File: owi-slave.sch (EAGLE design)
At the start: 6 parts, among them IC1 AT90S2313P

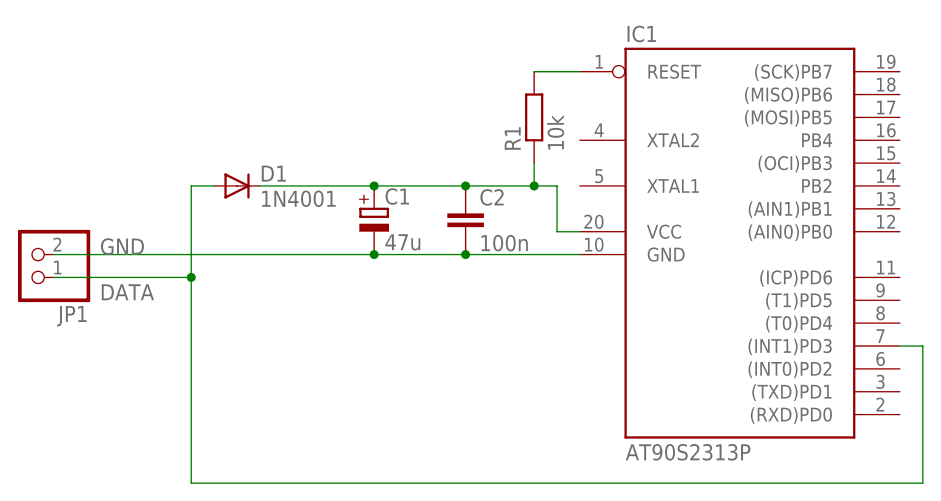
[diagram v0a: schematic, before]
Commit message: update readme and schematic (no bus-powered application at the moment)
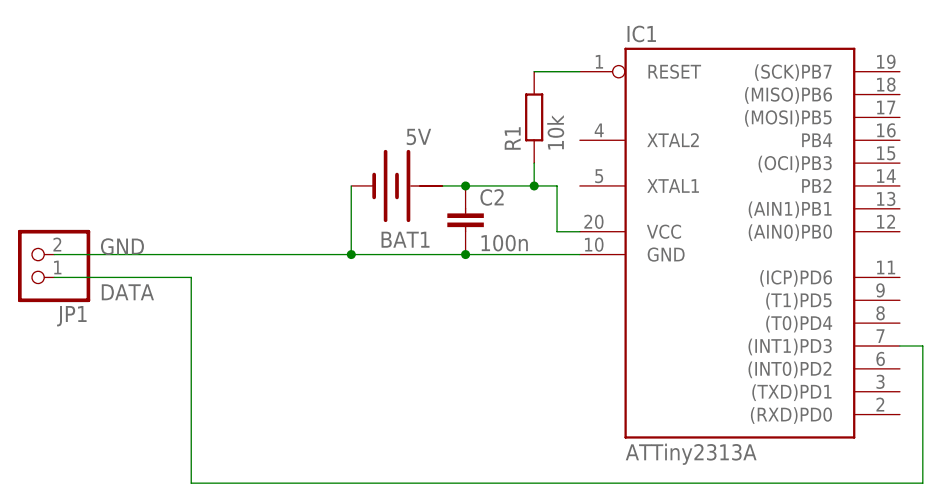
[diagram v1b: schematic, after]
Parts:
- removed C1: 47u, rcl:CPOL-EUE2,5-6E
- removed D1: 1N4001, diode:1N4004
- added BAT1: 5V, special:BATTERY
- IC1: value AT90S2313P -> ATTiny2313A
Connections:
- net DATA: no longer D1.A
- net GND: now also BAT1.-; no longer C1.-
- net N$1: now also BAT1.+; no longer C1.+, D1.C
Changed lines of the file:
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@@
 <?xml version="1.0" encoding="utf-8"?>
 <!DOCTYPE eagle SYSTEM "eagle.dtd">
-<eagle version="6.5.0">
+<eagle version="6.6.0">
 <drawing>
 <settings>
@@
 </classes>
 <parts>
-<part name="IC1" library="atmel" deviceset="AT90S2313" device="P"/>
-<part name="C1" library="rcl" deviceset="CPOL-EU" device="E2,5-6E" value="47u"/>
+<part name="IC1" library="atmel" deviceset="AT90S2313" device="P" value="ATTiny2313A"/>
 <part name="C2" library="resistor" deviceset="C-EU" device="025-024X044" value="100n"/>
-<part name="D1" library="diode" deviceset="1N4004" device="" value="1N4001"/>
 <part name="JP1" library="pinhead" deviceset="PINHD-1X2" device=""/>
 <part name="R1" library="resistor" deviceset="R-EU_" device="0207/10" value="10k"/>
+<part name="BAT1" library="special" deviceset="BATTERY" device="" value="5V"/>
 </parts>
 <sheets>
@@
 <instances>
 <instance part="IC1" gate="G$1" x="66.04" y="60.96"/>
-<instance part="C1" gate="G$1" x="25.4" y="66.04"/>
 <instance part="C2" gate="G$1" x="35.56" y="66.04"/>
-<instance part="D1" gate="1" x="10.16" y="68.58"/>
 <instance part="JP1" gate="G$1" x="-12.7" y="60.96" rot="R180"/>
 <instance part="R1" gate="G$1" x="43.18" y="76.2" rot="R90"/>
+<instance part="BAT1" gate="G$1" x="27.94" y="68.58" rot="R180"/>
 </instances>
 <busses>
@@
 <net name="N$1" class="0">
 <segment>
-<pinref part="D1" gate="1" pin="C"/>
-<pinref part="C1" gate="G$1" pin="+"/>
-<wire x1="12.7" y1="68.58" x2="25.4" y2="68.58" width="0.1524" layer="91"/>
 <pinref part="C2" gate="G$1" pin="1"/>
-<wire x1="25.4" y1="68.58" x2="35.56" y2="68.58" width="0.1524" layer="91"/>
 <wire x1="35.56" y1="68.58" x2="43.18" y2="68.58" width="0.1524" layer="91"/>
 <wire x1="43.18" y1="68.58" x2="45.72" y2="68.58" width="0.1524" layer="91"/>
@@
 <pinref part="IC1" gate="G$1" pin="VCC"/>
 <wire x1="45.72" y1="63.5" x2="48.26" y2="63.5" width="0.1524" layer="91"/>
-<junction x="25.4" y="68.58"/>
-<junction x="35.56" y="68.58"/>
 <pinref part="R1" gate="G$1" pin="1"/>
 <wire x1="43.18" y1="71.12" x2="43.18" y2="68.58" width="0.1524" layer="91"/>
 <junction x="43.18" y="68.58"/>
+<pinref part="BAT1" gate="G$1" pin="+"/>
+<wire x1="35.56" y1="68.58" x2="33.02" y2="68.58" width="0.1524" layer="91"/>
+<junction x="35.56" y="68.58"/>
 </segment>
 </net>
@@
 <pinref part="C2" gate="G$1" pin="2"/>
 <wire x1="48.26" y1="60.96" x2="35.56" y2="60.96" width="0.1524" layer="91"/>
-<pinref part="C1" gate="G$1" pin="-"/>
-<wire x1="35.56" y1="60.96" x2="25.4" y2="60.96" width="0.1524" layer="91"/>
+<label x="-5.08" y="60.96" size="1.778" layer="95"/>
+<pinref part="BAT1" gate="G$1" pin="-"/>
+<wire x1="22.86" y1="68.58" x2="22.86" y2="60.96" width="0.1524" layer="91"/>
+<wire x1="22.86" y1="60.96" x2="35.56" y2="60.96" width="0.1524" layer="91"/>
 <junction x="35.56" y="60.96"/>
-<junction x="25.4" y="60.96"/>
-<wire x1="25.4" y1="60.96" x2="-10.16" y2="60.96" width="0.1524" layer="91"/>
+<junction x="22.86" y="60.96"/>
 <pinref part="JP1" gate="G$1" pin="2"/>
-<label x="-5.08" y="60.96" size="1.778" layer="95"/>
+<wire x1="-10.16" y1="60.96" x2="22.86" y2="60.96" width="0.1524" layer="91"/>
 </segment>
 </net>
@@
 <wire x1="86.36" y1="35.56" x2="5.08" y2="35.56" width="0.1524" layer="91"/>
 <wire x1="5.08" y1="35.56" x2="5.08" y2="58.42" width="0.1524" layer="91"/>
-<pinref part="D1" gate="1" pin="A"/>
-<wire x1="5.08" y1="58.42" x2="5.08" y2="68.58" width="0.1524" layer="91"/>
-<wire x1="5.08" y1="68.58" x2="7.62" y2="68.58" width="0.1524" layer="91"/>
 <pinref part="JP1" gate="G$1" pin="1"/>
 <wire x1="-10.16" y1="58.42" x2="5.08" y2="58.42" width="0.1524" layer="91"/>
-<junction x="5.08" y="58.42"/>
 <label x="-5.08" y="55.88" size="1.778" layer="95"/>
 </segment>
